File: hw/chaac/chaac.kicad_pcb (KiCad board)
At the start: 2 copper layers, 71.1 x 63.5 mm, 84 parts, among them J1 windrain, J10 Therm, J11 FAN, J2 Conn_01x02, J3 UART, J4 Battery, J5 Power, J6 Light, J7 AM2315, J8 TC2030-CTX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

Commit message: Began placement for chaac
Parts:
- removed L2: 47nH, Inductor_SMD:L_0603_1608Metric
- removed R13, R14: 0, Resistor_SMD:R_0603_1608Metric
- added C31: 0.1uF, Capacitor_SMD:C_0603_1608Metric, F.Cu at (127.5, 93.5)
- added U7: XCL102, alvarop:XCL102, F.Cu at (112.7, 78.0)
- C11: value 22pF -> 0.1uF
- moved J3 92.9 mm to (131.5, 123.5), turned to 270 degrees
- moved U2 87.4 mm to (125.9, 111.0), turned to 180 degrees
- moved C24 87.2 mm to (120.5, 107.5), turned to 90 degrees
- moved C19 85.7 mm to (109.7, 114.3)
- moved C21 84.8 mm to (128.7, 115.6), turned to 270 degrees
- moved R8 81.6 mm to (117.3, 97.0)
- moved J2 81.4 mm to (145.0, 65.3), turned to 0 degrees
- moved C25 80.0 mm to (167.9, 94.5), turned to 270 degrees
- moved R9 79.3 mm to (117.3, 95.5)
- moved Y1 79.1 mm to (131.5, 113.6), turned to 270 degrees
- moved C23 78.2 mm to (131.5, 108.8)
- moved C2 78.2 mm to (141.5, 67.1), turned to 90 degrees
- moved U1 77.7 mm to (137.9, 67.1), turned to 270 degrees
- moved C5 77.2 mm to (134.6, 67.3), turned to 90 degrees
- moved U5 77.2 mm to (118.4, 100.6), turned to 90 degrees
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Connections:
- C11 pad 1: /GPS_RXD -> /BATT
- J3 pad 3: Net-(J3-Pad3) -> /UART_TX
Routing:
- net GND: track 31.6 -> 28.0 mm, vias 56 -> 53
- net /WDIR: track 4.67 -> 1.12 mm
- net Net-(U4-Pad9): track 2.64 -> 0.00 mm
- net /GPS_RXD: track 1.78 -> 0.00 mm
- net /WSPEED: track 2.89 -> 1.12 mm
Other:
- board size 71.1 x 63.5 mm -> 71.1 x 25.4 mm
- board text added: "RX"
- board text added: "TX"

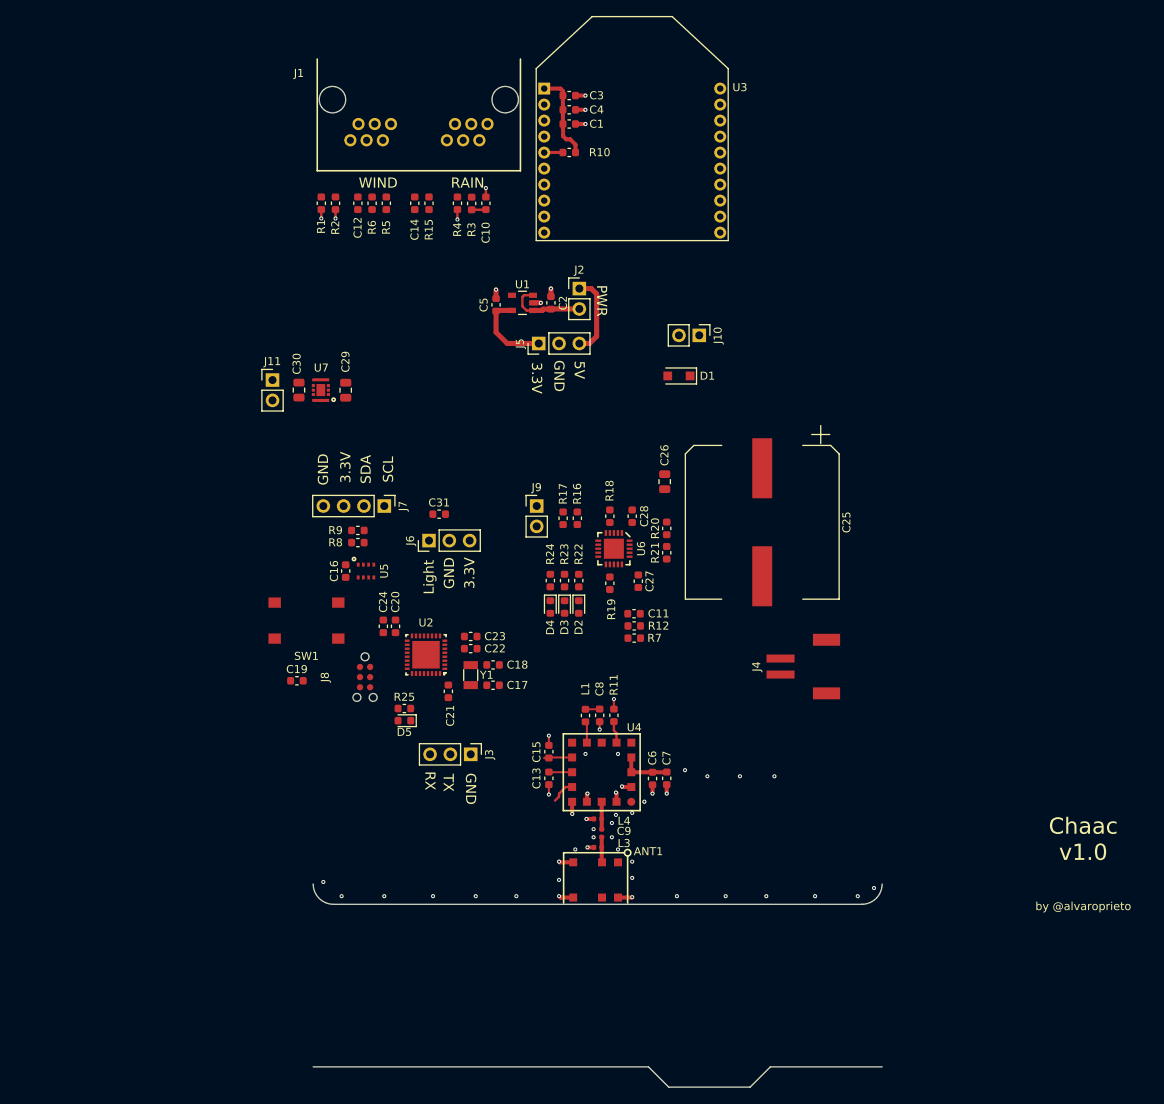
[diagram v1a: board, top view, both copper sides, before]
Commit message: Removed GPS, re-did placement
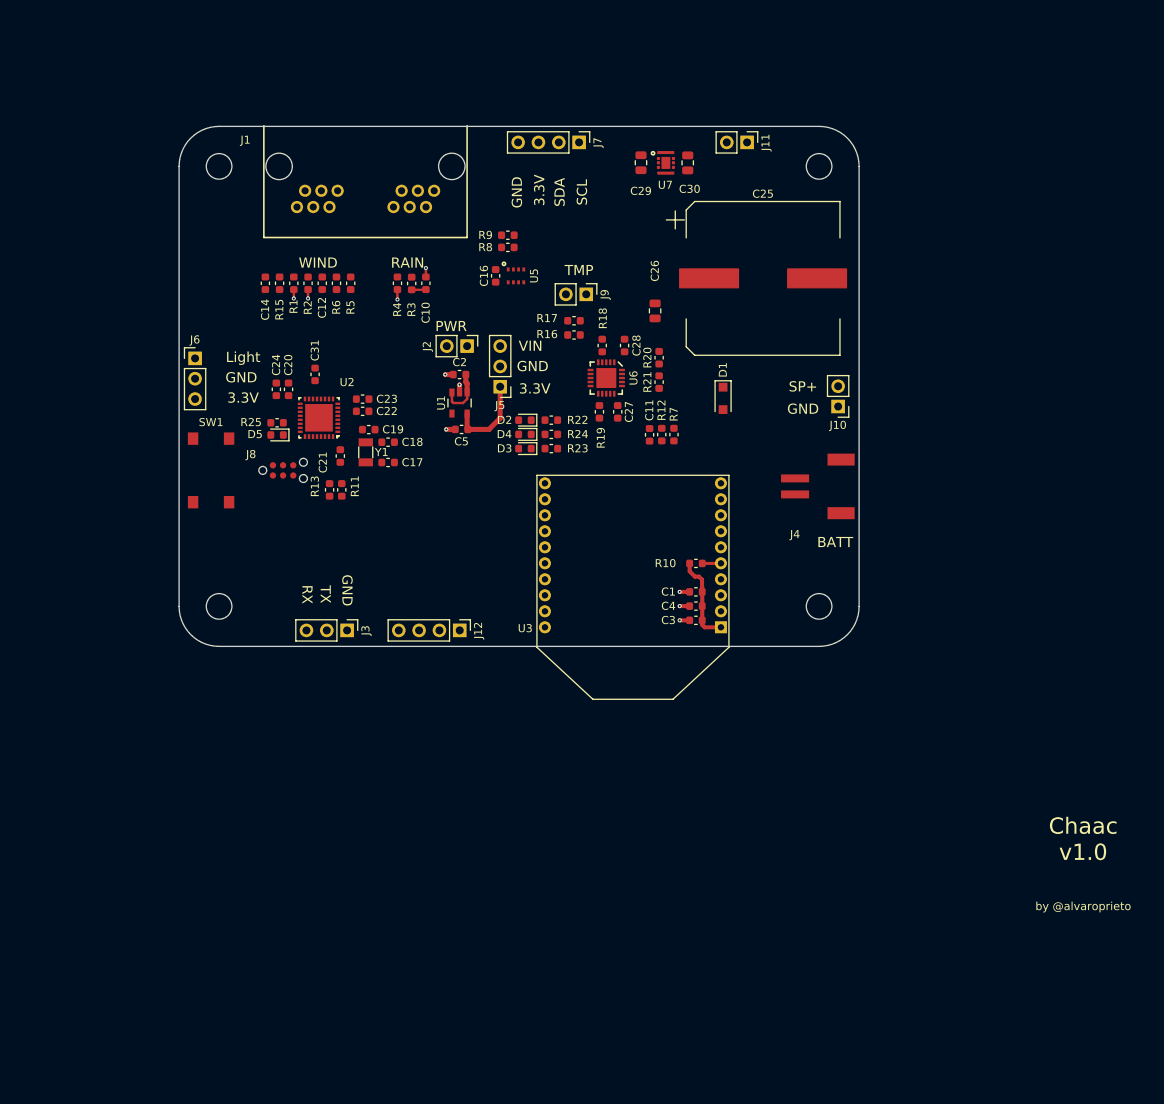
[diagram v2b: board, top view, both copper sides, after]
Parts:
- removed ANT1: SR4G008, alvarop:SR4G008
- removed C13, C15, C6, C8: 22pF, Capacitor_SMD:C_0603_1608Metric
- removed C7: 2.2uF, Capacitor_SMD:C_0603_1608Metric
- removed C9: 1.5pF, Capacitor_SMD:C_0402_1005Metric
- removed L1: 47nH, Inductor_SMD:L_0603_1608Metric
- removed L3: 12nH, Inductor_SMD:L_0402_1005Metric
- removed L4: DNP, Inductor_SMD:L_0402_1005Metric
- removed U4: M10578-A2, alvarop:M10578-A2
- added J12: AM2315, Connector_PinHeader_2.54mm:PinHeader_1x04_P2.54mm_Vertical, F.Cu at (130.1, 108.0)
- added R13: 0, Resistor_SMD:R_0603_1608Metric, F.Cu at (113.8, 90.4)
- added REF**: MountingHole_3.2mm_M3, MountingHole:MountingHole_3.2mm_M3, F.Cu at (175.0, 50.0)
- added REF**: MountingHole_3.2mm_M3, MountingHole:MountingHole_3.2mm_M3, F.Cu at (175.0, 105.0)
- added REF**: MountingHole_3.2mm_M3, MountingHole:MountingHole_3.2mm_M3, F.Cu at (100.0, 105.0)
- added REF**: MountingHole_3.2mm_M3, MountingHole:MountingHole_3.2mm_M3, F.Cu at (100.0, 50.0)
- R11: value 10k -> 0
- moved C3 67.5 mm to (159.6, 106.7), turned to 180 degrees
- moved J11 66.3 mm to (166.0, 47.0), turned to 270 degrees
- moved C4 64.0 mm to (159.6, 105.0), turned to 180 degrees
- moved C1 60.6 mm to (159.6, 103.2), turned to 180 degrees
- moved C30 56.3 mm to (158.6, 49.6), turned to 270 degrees
- moved R10 53.8 mm to (159.6, 99.6), turned to 180 degrees
- moved U7 51.6 mm to (155.8, 49.6), turned to 270 degrees
- moved J7 51.6 mm to (145.0, 47.0)
- moved U3 49.3 mm to (151.7, 98.6), turned to 0 degrees
- moved C29 46.6 mm to (152.7, 49.5), turned to 270 degrees
- moved R11 44.2 mm to (115.3, 90.4)
- moved U5 41.4 mm to (137.1, 63.7)
- moved C16 41.4 mm to (134.6, 63.7)
- moved R8 41.4 mm to (136.1, 60.1)
- moved R9 41.4 mm to (136.1, 58.6)
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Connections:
- J3 pad 2: /UART_RX -> Net-(J3-Pad2)
- R11 pad 1: GND -> /UART_RX
- R11 pad 2: Net-(R11-Pad2) -> /GPS_TX
- U2 pad 15: /GPS_FIX -> Net-(U2-Pad15)
- U2 pad 21: Net-(U2-Pad21) -> /LED1
- U2 pad 25: /GPS_TXD -> Net-(U2-Pad25)
- U2 pad 26: /GPS_SBY -> Net-(U2-Pad26)
- U2 pad 27: /LED1 -> Net-(U2-Pad27)
- U2 pad 31: Net-(U2-Pad31) -> /GPS_SBY
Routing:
- net GND: track 28.0 -> 9.17 mm, vias 53 -> 8
- net /VIN: track 10.3 -> 0.00 mm
- net +3V3: track 28.0 -> 21.7 mm
- net Net-(C2-Pad1): track 10.00 -> 6.47 mm
- net /GPS_SBY: track 3.51 -> 0.00 mm
- net Net-(C9-Pad2): track 3.44 -> 0.00 mm
- net Net-(ANT1-Pad2): track 3.17 -> 0.00 mm
- net Net-(U4-Pad6): track 3.06 -> 0.00 mm
- net /GPS_nRST: track 2.91 -> 0.00 mm
- net Net-(R11-Pad2): track 2.76 -> 0.00 mm
- net Net-(L1-Pad1): track 2.67 -> 0.00 mm
- net /GPS_TXD: track 1.79 -> 0.00 mm
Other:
- board size 71.1 x 25.4 mm -> 85 x 65 mm
- board text added: "BATT"
- board text added: "SP+"
- board text added: "TMP"
- board text added: "VIN"
- board text removed: "5V"

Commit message: Finished chaac 1.0 schematic and layout
Released to JLCPCB
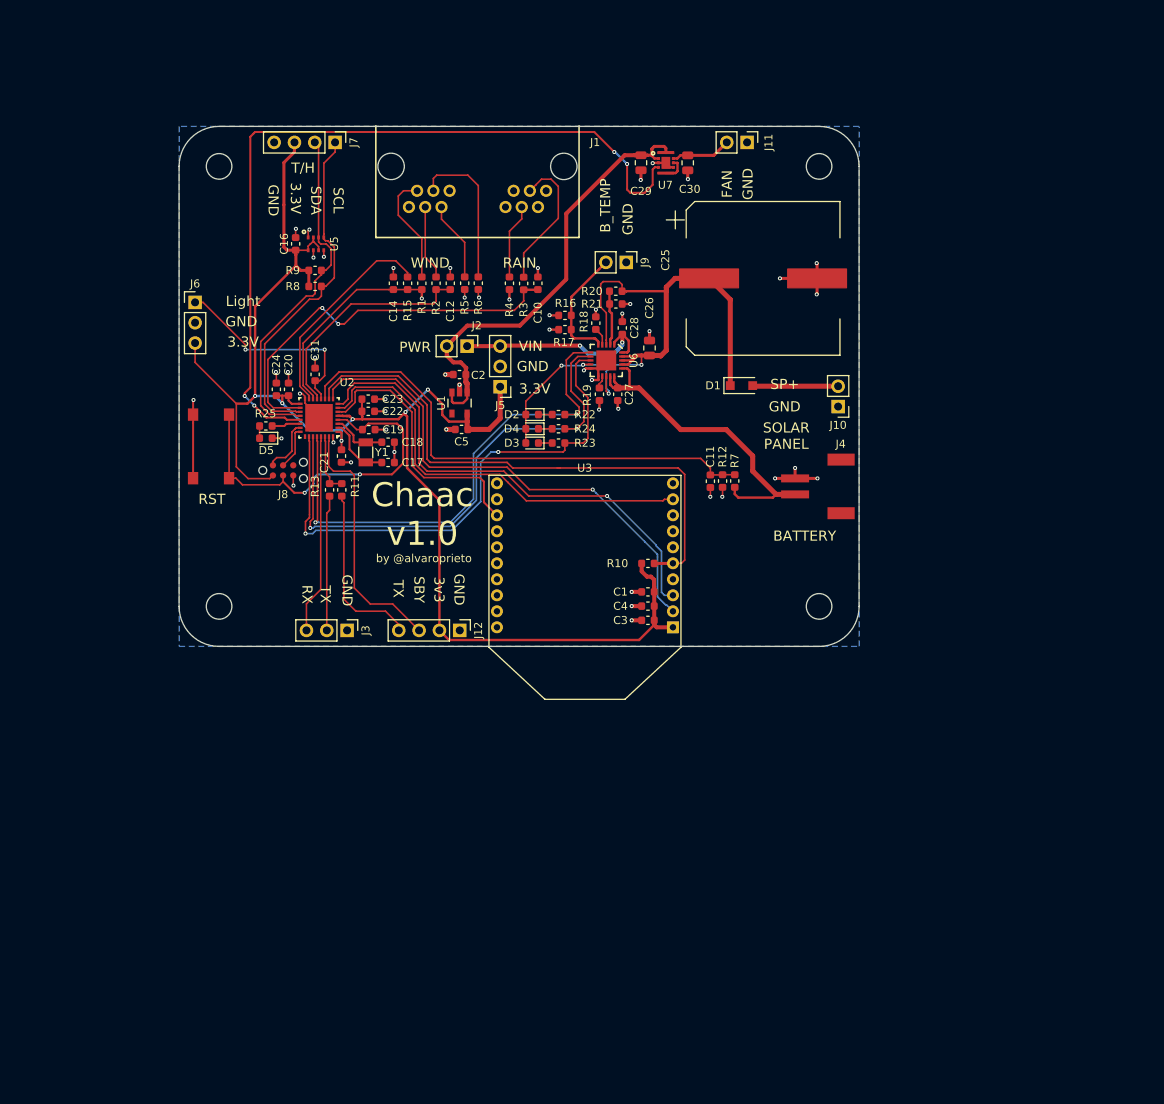
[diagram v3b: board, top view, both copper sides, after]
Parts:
- moved J7 30.5 mm to (114.5, 47.0)
- moved U5 25.3 mm to (112.1, 59.7)
- moved C16 25.3 mm to (109.6, 59.7)
- moved R8 24.6 mm to (112.0, 65.0)
- moved R9 24.5 mm to (112.0, 63.0)
- moved R6 17.7 mm to (132.4, 64.6)
- moved C14 16.0 mm to (121.8, 64.6)
- moved R1 16.0 mm to (125.3, 64.6)
- moved R15 16.0 mm to (123.6, 64.6)
- moved R2 16.0 mm to (127.1, 64.6)
- moved C12 16.0 mm to (128.9, 64.6)
- moved R5 14.2 mm to (130.7, 64.6)
- moved R4 14.0 mm to (136.3, 64.6)
- moved C10 14.0 mm to (139.8, 64.6)
- moved R3 14.0 mm to (138.1, 64.6)
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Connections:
- J12 pad 3: /GPS_TX -> /GPS_SBY
- J12 pad 4: /GPS_SBY -> /GPS_TX
- R15 pad 2: +3V3 -> /WDIR_EN
- R22 pad 1: Net-(R22-Pad1) -> /nPG
- R23 pad 1: Net-(R23-Pad1) -> /STAT1
- R24 pad 1: Net-(R24-Pad1) -> /STAT2
- U2 pad 11: /WDIR -> /BATT
- U2 pad 14: /BATT -> /WDIR
- U2 pad 15: Net-(U2-Pad15) -> /WDIR_EN
- U2 pad 21: /LED1 -> /FAN_EN
- U2 pad 22: Net-(U2-Pad22) -> /LED1
- U2 pad 26: Net-(U2-Pad26) -> /STAT1
- U2 pad 27: Net-(U2-Pad27) -> /STAT2
- U2 pad 28: /FAN_EN -> /nPG
- U6 pad 6: Net-(R22-Pad1) -> /nPG
- U6 pad 7: Net-(R24-Pad1) -> /STAT2
- U6 pad 8: Net-(R23-Pad1) -> /STAT1
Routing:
- net +3V3: track 21.7 -> 195.4 mm, vias 0 -> 6
- net /FAN_EN: track 0.00 -> 99.6 mm, vias 0 -> 4
- net /MCP_VIN: track 0.00 -> 84.8 mm, vias 0 -> 4
- net GND: track 9.17 -> 83.5 mm, vias 8 -> 50
- net /XB_nRST: track 2.35 -> 70.5 mm
- net /STAT1: track 0.00 -> 67.9 mm, vias 0 -> 2
- net /STAT2: track 0.00 -> 66.6 mm, vias 0 -> 2
- net /nPG: track 0.00 -> 64.9 mm, vias 0 -> 2
- net /XB_TX: track 0.00 -> 63.3 mm, vias 0 -> 1
- net /BATT: track 0.00 -> 63.3 mm
- net /XB_RX: track 0.00 -> 61.8 mm, vias 0 -> 1
- net /XB_nSBY: track 0.00 -> 53.7 mm
- net Net-(C2-Pad1): track 6.47 -> 56.3 mm
- net /RAIN: track 1.79 -> 49.6 mm, vias 0 -> 2
- net /nRST: track 0.00 -> 47.0 mm, vias 0 -> 2
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- added copper zone on B.Cu, net GND
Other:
- board text added: "3v3"
- board text added: "BATTERY"
- board text added: "B_TEMP"
- board text added: "FAN"
- board text added: "RST"
- board text added: "SBY"
- board text added: "SOLAR PANEL"
- board text added: "T/H"
- board text removed: "BATT"
- board text removed: "TMP"
